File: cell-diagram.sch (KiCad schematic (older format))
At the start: 12 parts, among them Q1 Q_NMOS_GSD, Q2 Q_PMOS_GSD, Q3 Q_NMOS_GSD, Q4 Q_PMOS_GSD, Q5 Q_NMOS_GSD, Q6 Q_NMOS_GSD, SW1 SW_SPST, SW2 SW_DPDT_x2, SW3 SW_SPST, SW4 SW_Push_Dual

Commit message: finish routing
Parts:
- removed BT1: Battery, symbol Device:Battery
- removed SW1: SW_SPST, symbol Switch:SW_SPST
- removed SW4: SW_Push_Dual, symbol Switch:SW_Push_Dual
- added D1, D10, D11, D12, D13, D14, D15, D16, D17, D18, D2, D3, D4, D5, D6, D7, D8, D9: LED, footprints:LED_1206_ReverseMountSquare1.5mm_HandSolder, symbol Device:LED
- added J1: USB_B_Micro, Connector_USB:USB_Micro-B_Wuerth_629105150521, symbol Connector:USB_B_Micro
- added Q10, Q11, Q7, Q8, Q9: Q_NMOS_GSD, Package_TO_SOT_SMD:SOT-23_Handsoldering, symbol Device:Q_NMOS_GSD
- added R1, R10, R11, R12, R13, R14, R15, R16, R17, R18, R2, R3, R4, R5, R6, R7, R8, R9: R_US, Resistor_SMD:R_0805_2012Metric_Pad1.15x1.40mm_HandSolder, symbol Device:R_US
- added R19: 10K, Resistor_SMD:R_0805_2012Metric_Pad1.15x1.40mm_HandSolder, symbol Device:R_US
- added SW1: SW_Write, Button_Switch_THT:SW_PUSH_6mm, symbol Switch:SW_Push
- added U1, U2: MC74VHC1G125, Package_TO_SOT_SMD:SOT-23-5, symbol #symbols:MC74VHC1G125
- R20: renamed from R1; value R_US -> 10K
- SW2: value SW_DPDT_x2 -> SW_Input; footprint (none) -> footprints:Switch_DPDT_THT_CK; Link (none) -> https://www.mouser.com/ProductDetail/JS202011CQN
- SW3: value SW_SPST -> SW_Enable; footprint (none) -> footprints:Switch_DPDT_THT_CK; Link (none) -> https://www.mouser.com/ProductDetail/JS102011SAQN
- renumbered Q2 to Q1, Q4 to Q2, Q5 to Q4, Q1 to Q5
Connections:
- net GND: now also Q3.2 (S), J1.5 (GND), Q10.2 (S), Q11.2 (S), Q7.2 (S), Q8.2 (S), Q9.2 (S), SW1.1, U1.3 (GND), U2.3 (GND); no longer Q3.3 (D)
- net Internal_R: now reaches Q1.1 (G), Q3.1 (G), Q4.3 (D)
- net Internal_R: now also Q2.3 (D), Q6.3 (D), Q9.1 (G); no longer Q2.2 (S), Q6.2 (S)
- net Internal_L: now reaches Q1.3 (D), Q2.1 (G), Q4.1 (G), Q5.3 (D)
- net Internal_L: now also Q3.3 (D), Q8.1 (G); no longer Q3.2 (S)
- net Enable: now reaches Q5.1 (G), Q6.1 (G), R20.1, SW3.2 (B)
- net Enable: now also Q7.1 (G)
- net External_L: now reaches Q5.2 (S)
- net External_L: now also Q10.1 (G), U2.4
- net at SW2.2 (B): now also U1.2
- net at SW2.5 (B): now also U2.2
- net VDD renamed VCC
- net VCC: now also Q2.2 (S), D1.2 (A), D10.2 (A), D11.2 (A), D12.2 (A), D13.2 (A), D14.2 (A), D15.2 (A), D16.2 (A), D17.2 (A), D18.2 (A), D2.2 (A), D3.2 (A), D4.2 (A), D5.2 (A), D6.2 (A), D7.2 (A), D8.2 (A), D9.2 (A), J1.1 (VBUS), R19.1, U1.5 (VCC), U2.5 (VCC); no longer Q2.3 (D)
- new net: R19.2, SW1.2, U1.1, U2.1
- new net: Q8.3 (D), R5.2, R6.2, R7.2, R8.2
- new net: D8.1 (K), R8.1
- new net: D7.1 (K), R7.1
- new net: D6.1 (K), R6.1
- new net: D5.1 (K), R5.1
- new net: Q9.3 (D), R10.2, R11.2, R12.2, R9.2
- new net: D12.1 (K), R12.1
- new net: D11.1 (K), R11.1
- new net: D10.1 (K), R10.1
- new net: D9.1 (K), R9.1
- new net: Q10.3 (D), R13.2, R14.2, R15.2
- new net: D15.1 (K), R15.1
- new net: D14.1 (K), R14.1
- new net: D13.1 (K), R13.1
- new net: Q11.3 (D), R16.2, R17.2, R18.2
- new net: D18.1 (K), R18.1
- new net: D17.1 (K), R17.1
- new net: D16.1 (K), R16.1
- new net: Q7.3 (D), R1.2, R2.2, R3.2, R4.2
- new net: D4.1 (K), R4.1
- new net: D3.1 (K), R3.1
- new net: D2.1 (K), R2.1
- new net: D1.1 (K), R1.1
- new net External_R: Q11.1 (G), Q6.2 (S), U1.4
- no-connect marks 0 -> 4
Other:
- note added: "Reverse Mounted LEDs"
- moved on the sheet: Q1, Q2, Q3, Q4, Q5, Q6, R20, SW2A, SW2B, SW3

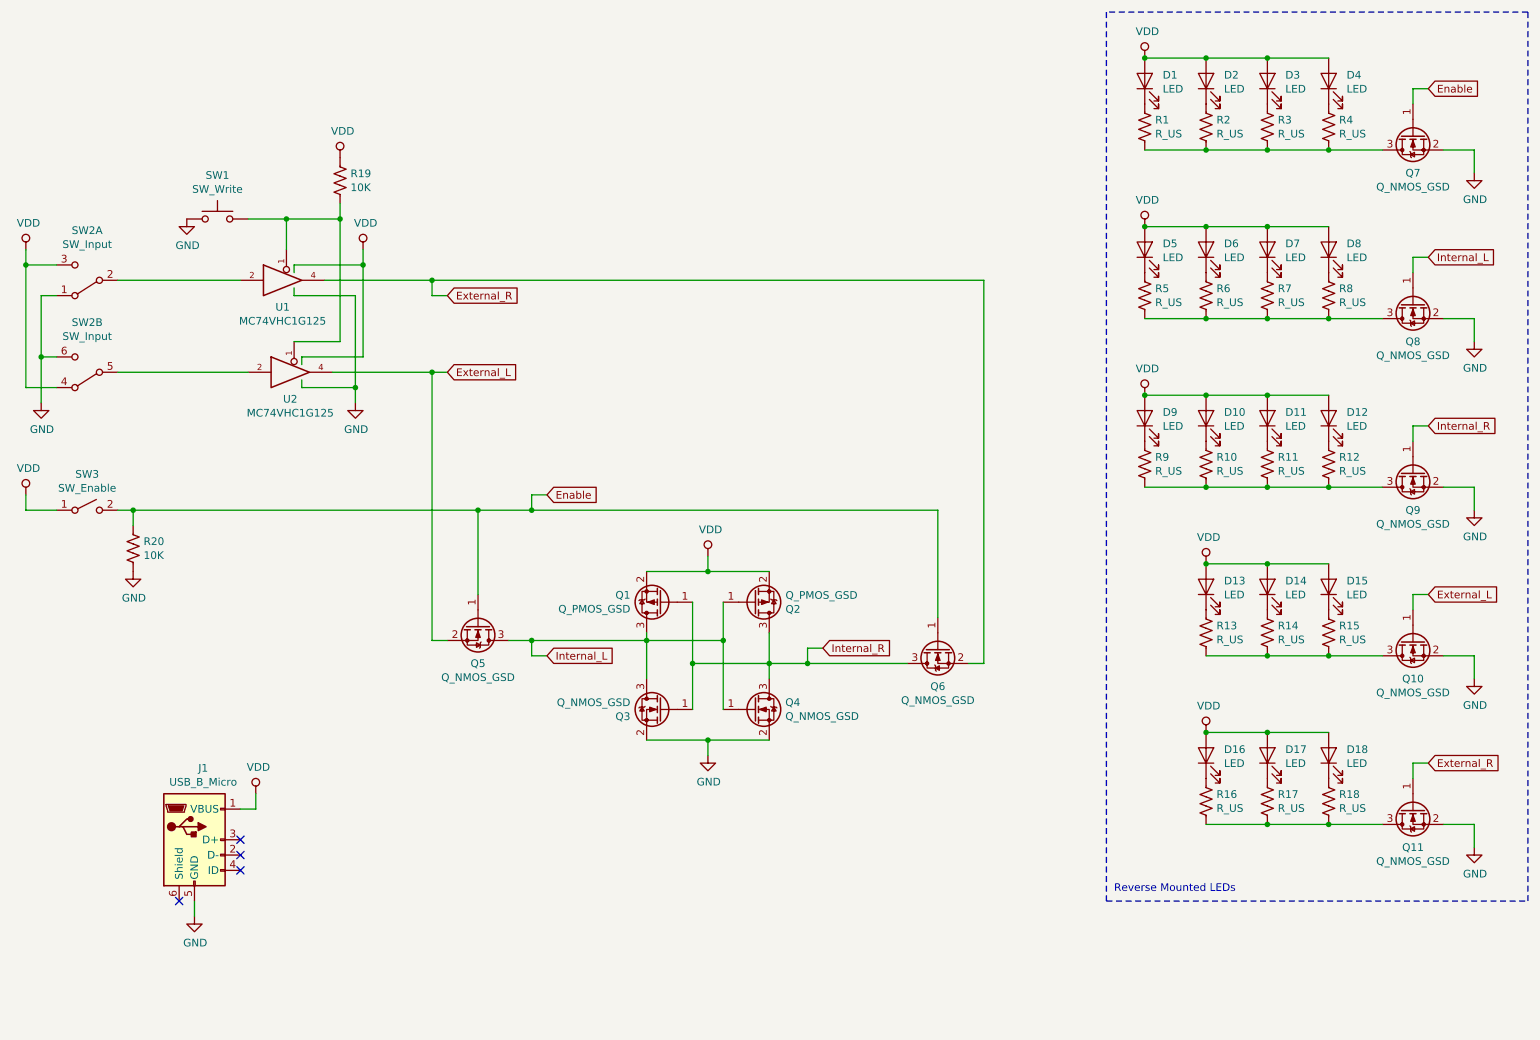
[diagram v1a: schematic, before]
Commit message: add optional power regulation
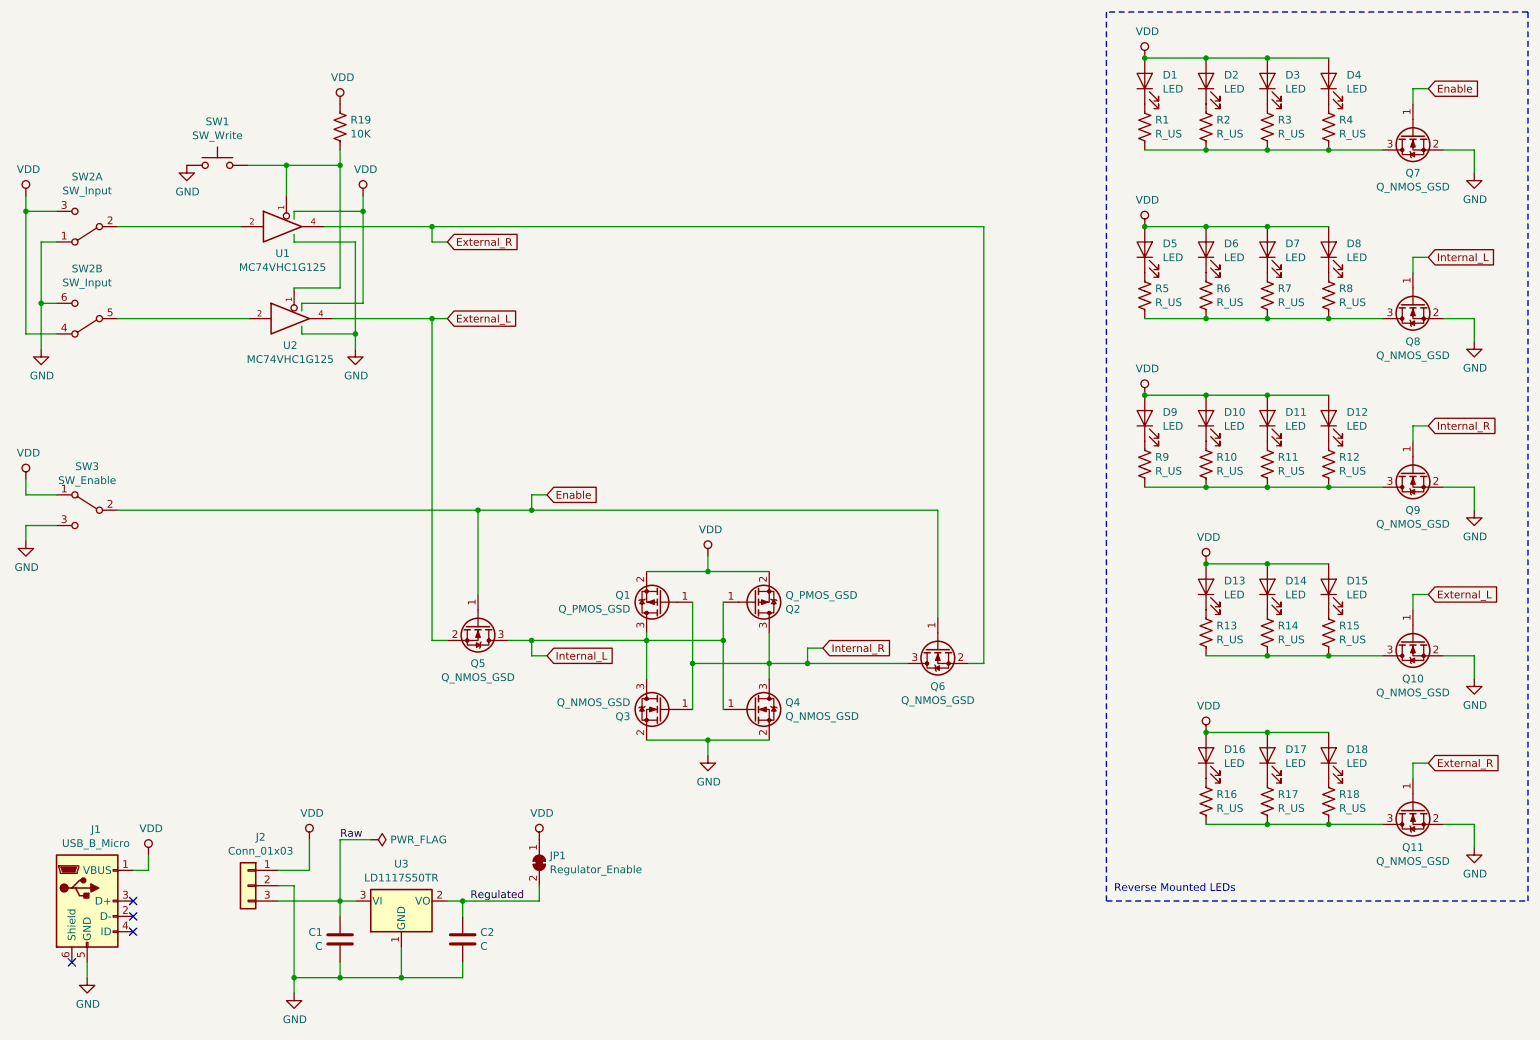
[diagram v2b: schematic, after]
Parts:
- removed R20: 10K, Resistor_SMD:R_0805_2012Metric_Pad1.15x1.40mm_HandSolder, symbol Device:R_US
- removed SW3: SW_Enable, footprints:Switch_DPDT_THT_CK, symbol Switch:SW_SPST
- added C1, C2: C, Capacitor_SMD:C_0805_2012Metric_Pad1.15x1.40mm_HandSolder, symbol Device:C
- added J2: Conn_01x03, Connector_PinHeader_2.54mm:PinHeader_1x03_P2.54mm_Vertical, symbol Connector_Generic:Conn_01x03
- added JP1: Regulator_Enable, Jumper:SolderJumper-2_P1.3mm_Bridged_RoundedPad1.0x1.5mm, symbol Jumper:SolderJumper_2_Bridged
- added SW3: SW_Enable, #footprints:Switch_DPDT_THT_CK, symbol Switch:SW_SPDT
- added U3: LD1117S50TR, Package_TO_SOT_SMD:SOT-223-3_TabPin2, symbol Regulator_Linear:LD1117S50TR_SOT223
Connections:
- net Enable: now also SW3.2 (B)
- net GND: now also C1.2, C2.2, J2.2 (Pin_2), SW3.3 (C), U3.1 (GND)
- net VCC: now also J2.1 (Pin_1), JP1.1 (A), SW3.1 (A)
- new net Raw: C1.1, J2.3 (Pin_3), U3.3 (VI)
- new net Regulated: C2.1, JP1.2 (B), U3.2 (VO)
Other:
- moved on the sheet: J1, R19, SW1, SW2A, SW2B, U1, U2

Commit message: make some cosmetic improvements
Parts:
- C1, C2: Link (none) -> https://www.mouser.com/ProductDetail/C0805C106K9PACTU
- D1, D10, D11, D12, D13, D14, D15, D16, D17, D18, D2, D3, D4, D5, D6, D7, D8, D9: value LED -> (none); footprint footprints:LED_1206_ReverseMountSquare1.5mm_HandSolder -> #footprints:LED_1206_ReverseMountSquare1.5mm_HandSolder; Link (none) -> https://www.mouser.com/ProductDetail/859-LTST-C230KSKT
- J1: footprint Connector_USB:USB_Micro-B_Wuerth_629105150521 -> Connector_USB:USB_Micro-B_Molex-105017-0001; Link (none) -> https://www.mouser.com/ProductDetail/105017-0001
- J2: value Conn_01x03 -> PowerHeader; footprint Connector_PinHeader_2.54mm:PinHeader_1x03_P2.54mm_Vertical -> #footprints:PowerHeader_P2.54mm
- Q1, Q2: value Q_PMOS_GSD -> PMOS_GSD; Link (none) -> https://www.mouser.com/ProductDetail/BSS84-7-F
- Q10, Q11, Q3, Q4, Q5, Q6, Q7, Q8, Q9: value Q_NMOS_GSD -> NMOS_GSD; Link (none) -> https://www.mouser.com/ProductDetail/2N7002-7-F
- R1, R10, R11, R12, R13, R14, R15, R16, R17, R18, R2, R3, R4, R5, R6, R7, R8, R9: value R_US -> (none)
- SW2: footprint footprints:Switch_DPDT_THT_CK -> #footprints:Switch_DPDT_THT_CK
- SW3: Link https://www.mouser.com/ProductDetail/JS102011SAQN -> https://www.mouser.com/ProductDetail/JS202011CQN
- U1, U2: Link (none) -> https://www.mouser.com/ProductDetail/MC74VHC1G125DBVT1G
- U3: Link (none) -> https://www.mouser.com/ProductDetail/LD1117S50TR
